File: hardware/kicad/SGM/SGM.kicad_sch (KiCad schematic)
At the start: 0 parts

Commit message: Implement power input stage
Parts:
- added C1: 10uF 50V X7R, Capacitor_SMD:C_1206_3216Metric, symbol Device:C
- added C2: 100nF 50V X7R, Capacitor_SMD:C_0603_1608Metric, symbol Device:C
- added C3: 100nF bootstrap, Capacitor_SMD:C_0603_1608Metric, symbol Device:C
- added C4: 22uF 10V X7R, Capacitor_SMD:C_1206_3216Metric, symbol Device:C
- added D1: SMBJ24A, Diode_SMD:D_SMB, symbol Device:D_TVS
- added D2: 12V VGS clamp, Diode_SMD:D_SOD-123, symbol Device:D_TVS
- added F1: 2A, symbol Device:Fuse
- added J1: BATTERY IN, TerminalBlock:TerminalBlock_bornier-2_P5.08mm, symbol Connector_Generic:Conn_01x02
- added L1: 4.7uH >=3A, Inductor_SMD:L_6.0x6.0_H3.0, symbol Device:L
- added Q1: AO3407A, Package_TO_SOT_SMD:SOT-23, symbol Device:Q_PMOS
- added R1: 100k, Resistor_SMD:R_0603_1608Metric, symbol Device:R
- added U1: AP63203WU-7, Package_TO_SOT_SMD:TSOT-23-6, symbol Regulator_Switching:AP63203WU
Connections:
- new net: D2.1 (A1), Q1.G, R1.1
- new net: D1.2 (A2), D2.2 (A2), Q1.D, R1.2
- new net: C1.1, Q1.S, U1.2 (EN), U1.3 (IN)
- new net: D1.1 (A1), F1.2
- new net +3V3: C4.1, L1.2, U1.5 (SW)
- new net GND: C1.2, C2.2, C3.2, C4.2, F1.1, J1.1 (Pin_1), J1.2 (Pin_2)
- new net SW: C3.1, L1.1, U1.6 (BST)
- new net VIN_PROTECTED: C2.1
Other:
- note added: "AP63203WU-7 fixed 3.3V output; FB tied directly to +3V3"
- title: (none) -> SmartGarageMeter Power Input

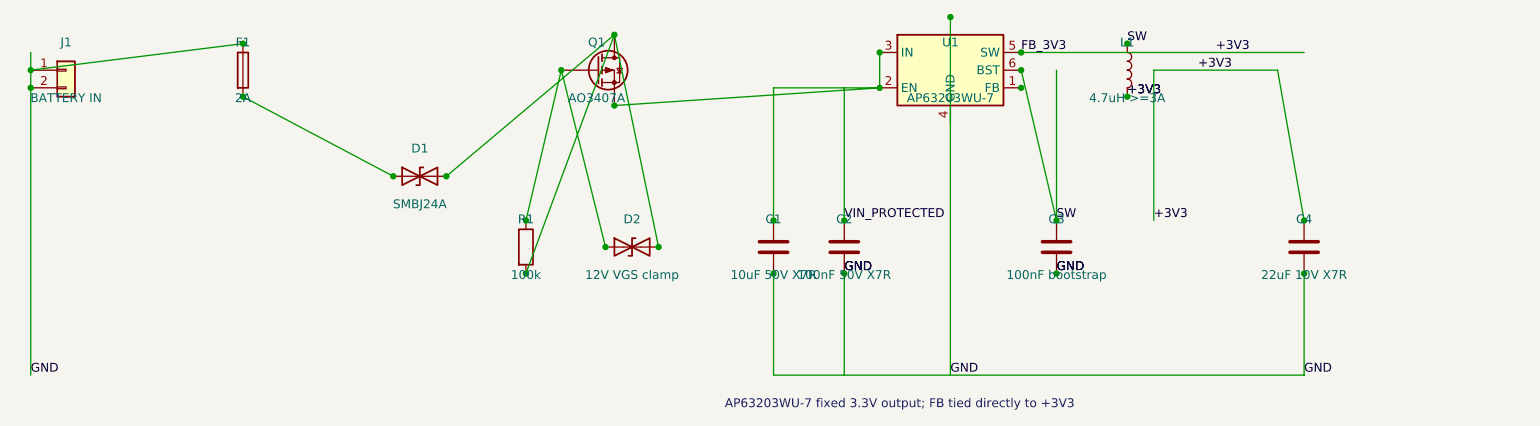
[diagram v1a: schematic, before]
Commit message: 002
hardware: add initial power input schematic
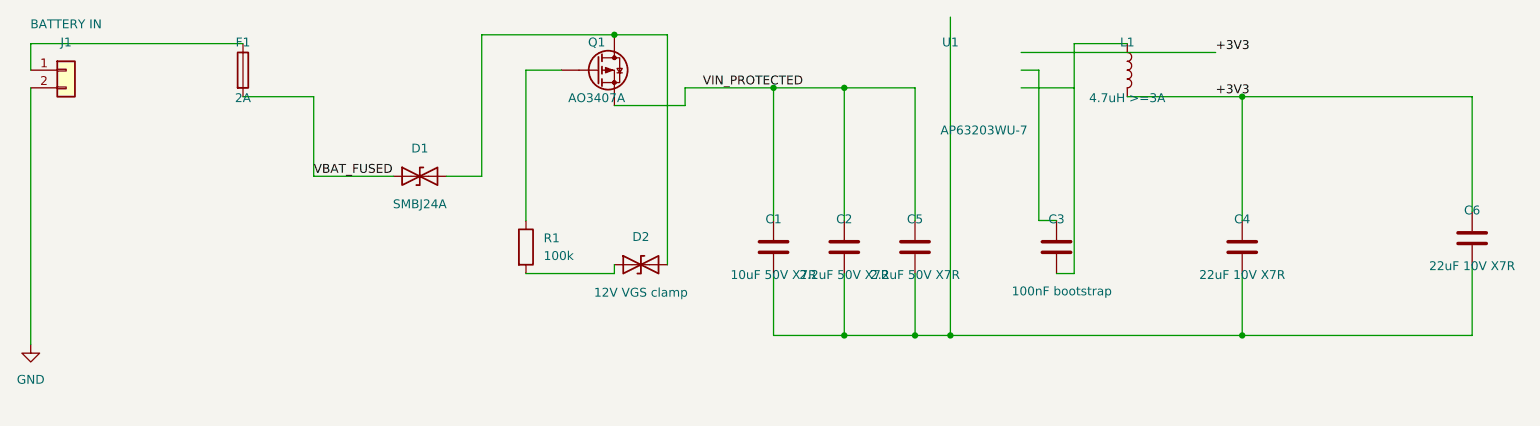
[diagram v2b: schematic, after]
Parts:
- added C5: 2.2uF 50V X7R, Capacitor_SMD:C_0603_1608Metric, symbol Device:C
- added C6: 22uF 10V X7R, Capacitor_SMD:C_1206_3216Metric, symbol Device:C
- C2: value 100nF 50V X7R -> 2.2uF 50V X7R
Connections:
- net +3V3: now also C6.1; no longer U1.5 (SW)
- net GND: no longer C1.2, C2.2, C3.2, C4.2, F1.1, J1.1 (Pin_1)
- net VIN_PROTECTED: now also C1.1, Q1.S, C5.1
- net at Q1.G, R1.1: no longer D2.1 (A1)
- net at D1.2 (A2), D2.2 (A2), Q1.D: no longer R1.2
- net VBAT_FUSED: now reaches D1.1 (A1), F1.2
- removed net SW: C3.1, L1.1, U1.6 (BST)
- new net: C1.2, C2.2, C4.2, C5.2, C6.2
- new net: F1.1, J1.1 (Pin_1)
- new net: C3.2, L1.1
- new net: D2.1 (A1), R1.2
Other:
- note removed: "AP63203WU-7 fixed 3.3V output; FB tied directly to +3V3"
- moved on the sheet: C4, D2

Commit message: hardware: finalize power input stage
hardware: finalize power input stage
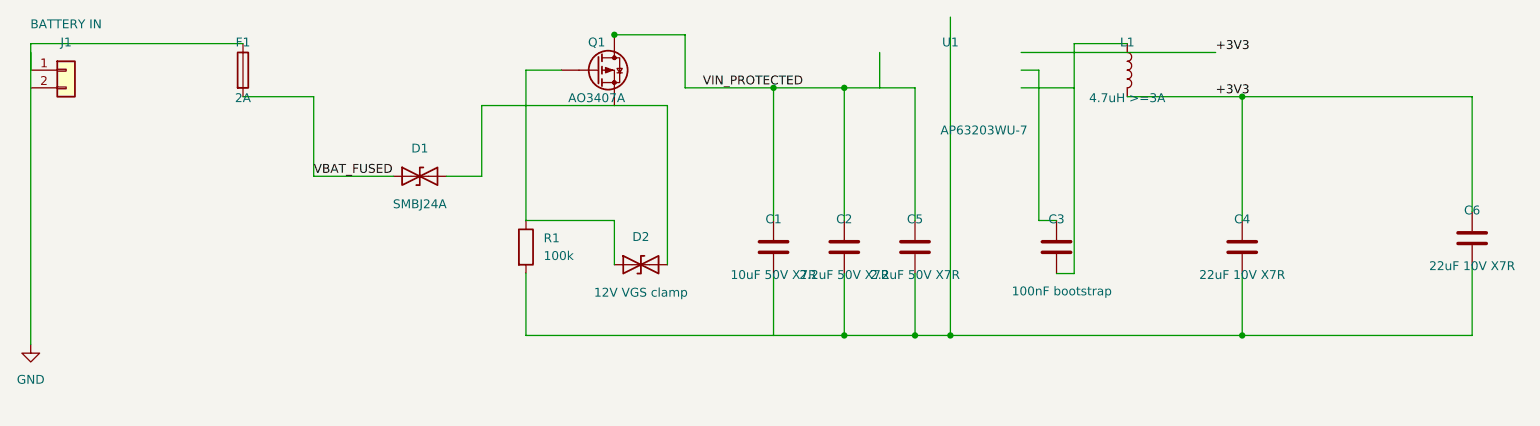
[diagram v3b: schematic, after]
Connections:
- net GND: now also F1.1, J1.1 (Pin_1); no longer J1.2 (Pin_2)
- net VIN_PROTECTED: now also Q1.D; no longer Q1.S
- net at C1.2, C2.2, C4.2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: now also R1.2
- net at Q1.G, R1.1: now also D2.1 (A1)
- net at D1.2 (A2), D2.2 (A2): now also Q1.S; no longer Q1.D
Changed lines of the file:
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@@
 	(wire
 		(pts
-			(xy 20.32 78.74) (xy 20.32 115.57)
-		)
-		(stroke
-			(width 0)
-			(type default)
-		)
-	)
-	(wire
-		(pts
-			(xy 85.09 71.12) (xy 104.14 71.12)
+			(xy 20.32 73.66) (xy 20.32 115.57)
+		)
+		(stroke
+			(width 0)
+			(type default)
+		)
+	)
+	(wire
+		(pts
+			(xy 85.09 81.28) (xy 104.14 81.28)
 		)
 		(stroke
@@
 	(wire
 		(pts
-			(xy 111.76 71.12) (xy 104.14 71.12)
+			(xy 111.76 81.28) (xy 104.14 81.28)
 		)
 		(stroke
@@
 	(wire
 		(pts
-			(xy 104.14 105.41) (xy 104.14 104.14)
-		)
-		(stroke
-			(width 0)
-			(type default)
-		)
-	)
-	(wire
-		(pts
-			(xy 111.76 104.14) (xy 111.76 71.12)
+			(xy 104.14 104.14) (xy 104.14 97.79)
+		)
+		(stroke
+			(width 0)
+			(type default)
+		)
+	)
+	(wire
+		(pts
+			(xy 111.76 104.14) (xy 111.76 81.28)
 		)
 		(stroke
@@
 	(wire
 		(pts
-			(xy 104.14 105.41) (xy 91.44 105.41)
+			(xy 104.14 97.79) (xy 91.44 97.79)
 		)
 		(stroke
@@
 	(wire
 		(pts
-			(xy 114.3 81.28) (xy 114.3 78.74)
+			(xy 114.3 71.12) (xy 114.3 78.74)
+		)
+		(stroke
+			(width 0)
+			(type default)
+		)
+	)
+	(wire
+		(pts
+			(xy 91.44 105.41) (xy 91.44 114.3)
+		)
+		(stroke
+			(width 0)
+			(type default)
+		)
+	)
+	(wire
+		(pts
+			(xy 91.44 114.3) (xy 127 114.3)
+		)
+		(stroke
+			(width 0)
+			(type default)
+		)
+	)
+	(wire
+		(pts
+			(xy 142.24 73.66) (xy 142.24 78.74)
 		)
 		(stroke
@@
 	(wire
 		(pts
-			(xy 85.09 91.44) (xy 85.09 71.12)
+			(xy 85.09 91.44) (xy 85.09 81.28)
 		)
 		(stroke
@@
 	(wire
 		(pts
-			(xy 104.14 81.28) (xy 114.3 81.28)
-		)
-		(stroke
+			(xy 104.14 71.12) (xy 114.3 71.12)
+		)
+		(stroke
